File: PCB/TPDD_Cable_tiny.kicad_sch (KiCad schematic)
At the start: 5 parts, among them J1 Conn_01x07, J2 TPDD, Q1 DTA114E, Q2 DTA114E, Q3 DTA114E

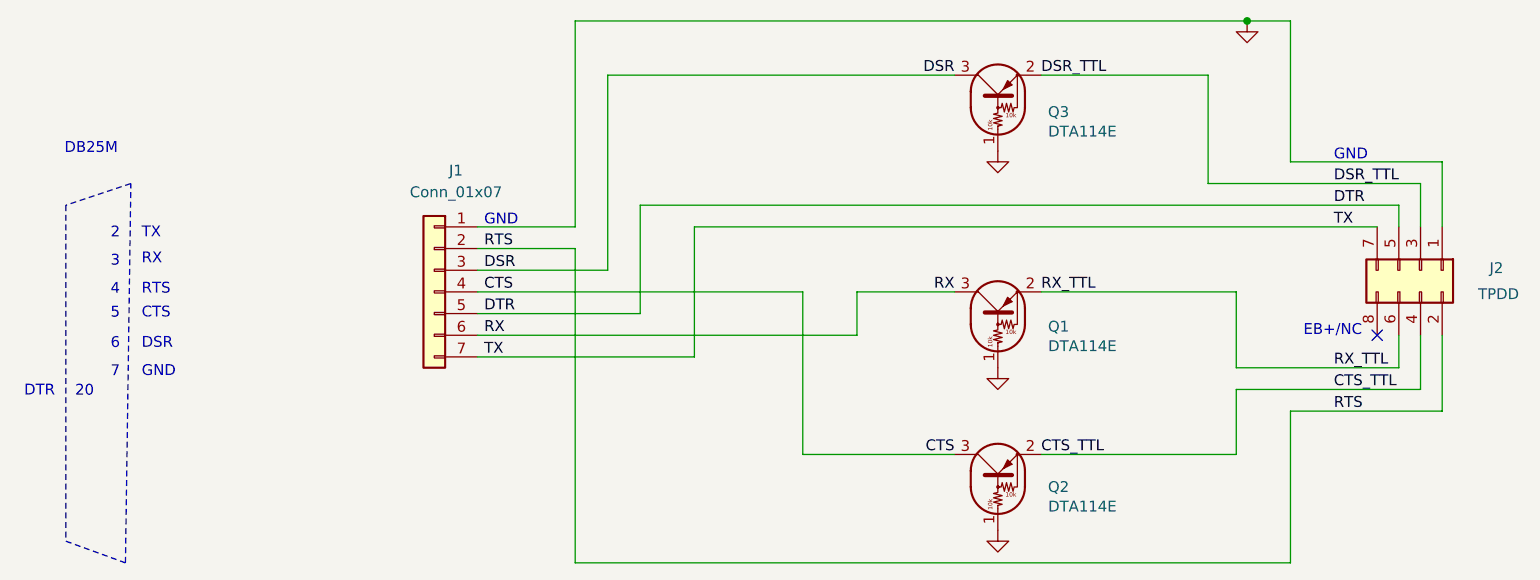
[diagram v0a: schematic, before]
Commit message: schematics notes text
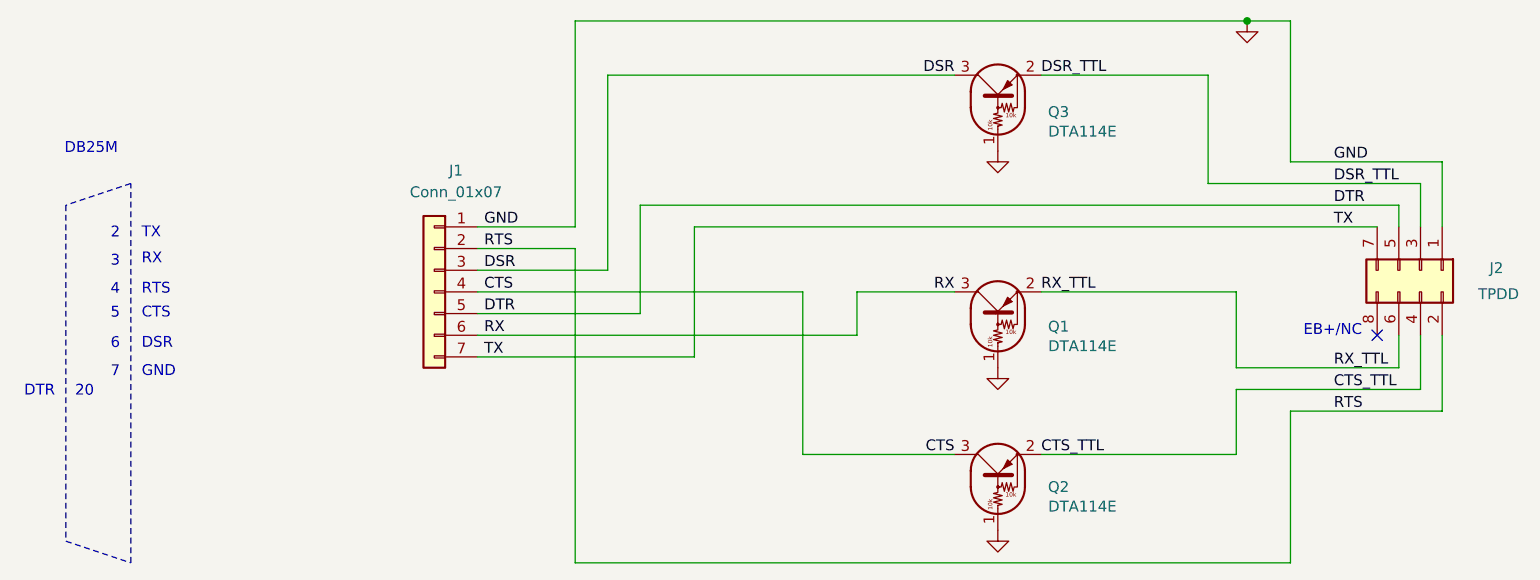
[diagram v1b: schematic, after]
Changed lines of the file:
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@@
 	(polyline
 		(pts
-			(xy 66.675 120.65) (xy 67.31 76.2)
+			(xy 67.31 120.65) (xy 67.31 76.2)
 		)
 		(stroke
@@
 	(polyline
 		(pts
-			(xy 59.69 118.11) (xy 66.675 120.65)
+			(xy 59.69 118.11) (xy 67.31 120.65)
 		)
 		(stroke
@@
 		)
 	)
+	(text "2"
+		(exclude_from_sim no)
+		(at 66.04 82.804 0)
+		(effects
+			(font
+				(size 1.27 1.27)
+			)
+			(justify right bottom)
+		)
+	)
+	(text "DB25M"
+		(exclude_from_sim no)
+		(at 65.786 72.898 0)
+		(effects
+			(font
+				(size 1.27 1.27)
+			)
+			(justify right bottom)
+		)
+	)
+	(text "20"
+		(exclude_from_sim no)
+		(at 62.992 101.346 0)
+		(effects
+			(font
+				(size 1.27 1.27)
+			)
+			(justify right bottom)
+		)
+	)
+	(text "TX"
+		(exclude_from_sim no)
+		(at 68.58 82.042 0)
+		(effects
+			(font
+				(size 1.27 1.27)
+			)
+			(justify left)
+		)
+	)
 	(text "GND"
 		(exclude_from_sim no)
-		(at 208.28 73.66 0)
-		(effects
-			(font
-				(size 1.27 1.27)
-			)
-			(justify left bottom)
-		)
-	)
-	(text "2"
-		(exclude_from_sim no)
-		(at 66.04 82.804 0)
-		(effects
-			(font
-				(size 1.27 1.27)
-			)
-			(justify right bottom)
-		)
-	)
-	(text "DB25M"
-		(exclude_from_sim no)
-		(at 65.786 72.898 0)
-		(effects
-			(font
-				(size 1.27 1.27)
-			)
-			(justify right bottom)
-		)
-	)
-	(text "20"
-		(exclude_from_sim no)
-		(at 62.992 101.346 0)
-		(effects
-			(font
-				(size 1.27 1.27)
-			)
-			(justify right bottom)
-		)
-	)
-	(text "TX"
-		(exclude_from_sim no)
-		(at 68.58 82.042 0)
+		(at 68.58 98.298 0)
 		(effects
 			(font
@@
 		)
 	)
-	(text "GND"
-		(exclude_from_sim no)
-		(at 68.58 98.298 0)
-		(effects
-			(font
-				(size 1.27 1.27)
-			)
-			(justify left)
-		)
-	)
 	(text "6"
 		(exclude_from_sim no)
@@
 			)
 			(justify right bottom)
-		)
-	)
-	(text "GND"
-		(exclude_from_sim no)
-		(at 108.712 81.28 0)
-		(effects
-			(font
-				(size 1.27 1.27)
-			)
-			(justify left bottom)
 		)
 	)
@@
 		)
 	)
+	(label "GND"
+		(at 208.28 73.66 0)
+		(fields_autoplaced yes)
+		(effects
+			(font
+				(size 1.27 1.27)
+			)
+			(justify left bottom)
+		)
+	)
 	(label "DSR"
 		(at 108.712 86.36 0)
@@
 		(fields_autoplaced yes)
 		(effects
+			(font
+				(size 1.27 1.27)
+			)
+			(justify left bottom)
+		)
+	)
+	(label "GND"
+		(at 108.712 81.28 0)
+		(fields_autoplaced yes)
+		(effects
